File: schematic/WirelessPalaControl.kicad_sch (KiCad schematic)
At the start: 18 parts, among them J1 6P4C, J2 MCU UART, J3 WeMos_mini_Hat_Left, J4 WeMos_mini_Hat_Right, U1 SI8621

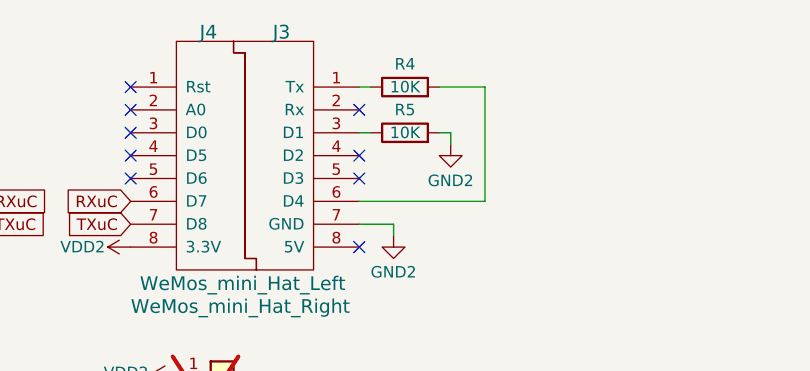
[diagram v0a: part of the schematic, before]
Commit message: Change R4 to 2K
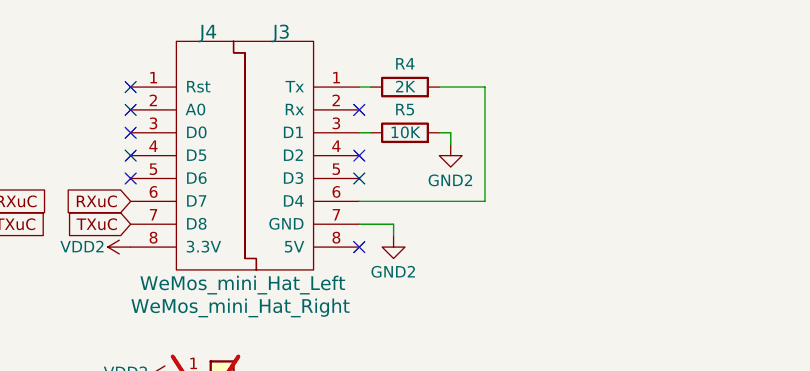
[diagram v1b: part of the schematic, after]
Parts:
- R4: value 10K -> 2K; LCSC C17414 -> C17604
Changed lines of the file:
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@@
 			)
 		)
-		(property "Value" "10K"
+		(property "Value" "2K"
 			(at 142.24 22.86 90)
 			(effects
@@
 			)
 		)
-		(property "LCSC" "C17414"
+		(property "LCSC" "C17604"
 			(at 142.24 22.86 90)
 			(effects
